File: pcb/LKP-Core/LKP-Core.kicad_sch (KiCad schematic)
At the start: 34 parts, among them J1 Intercon L, J2 Intercon R, J3 Power JST PH, J4 IO, J5 SWD, J6 WS281x, U1 CY8C4246AZI-M445

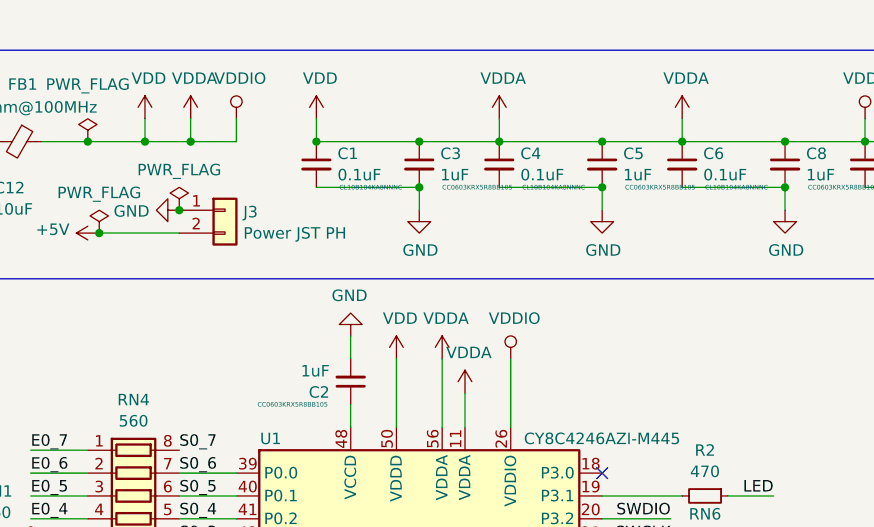
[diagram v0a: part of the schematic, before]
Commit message: Minor adjustments to LKP-Core and release v1.3
- Move LKP-Core to KiCad 7
- Add teardrop to everything except on intercon connectors.
- Use regular LED footprint instead of the accidentally added castellated one (somewhat a duplicate of handsoldering but slightly larger)
- Move to mainline PSoC symbol
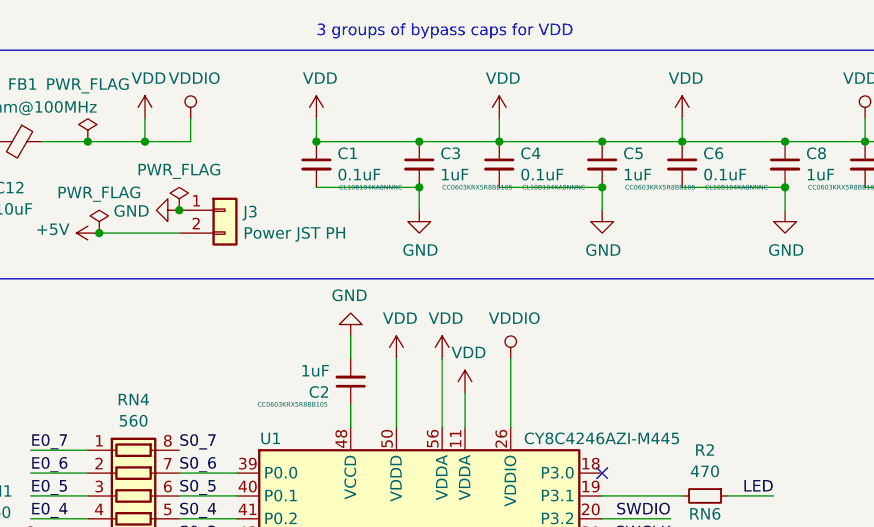
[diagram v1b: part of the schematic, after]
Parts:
- D2: footprint LED_SMD:LED_0805_2012Metric_Castellated -> LED_SMD:LED_0805_2012Metric
- J4: symbol Connector:Conn_01x04_Male -> Connector:Conn_01x04_Pin
- J5: symbol Connector:Conn_01x05_Male -> Connector:Conn_01x05_Pin
- J6: symbol Connector:Conn_01x02_Male -> Connector:Conn_01x02_Pin
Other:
- note added: "3 groups of bypass caps for VDD"
